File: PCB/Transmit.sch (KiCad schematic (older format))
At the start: 1 part

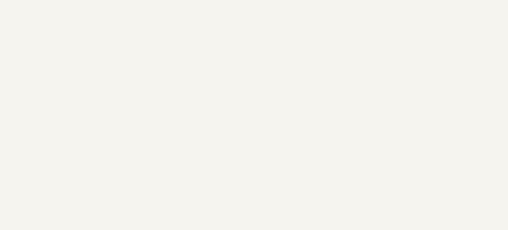
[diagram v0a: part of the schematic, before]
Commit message: Add diode pair to library
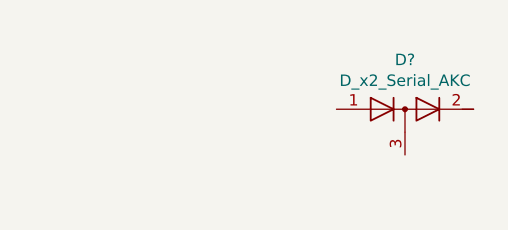
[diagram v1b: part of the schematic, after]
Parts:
- added D?: D_x2_Serial_AKC, Parts:MMBD7000L, symbol Device:D_x2_Serial_AKC
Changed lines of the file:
@@
 $Descr A4 11693 8268
 encoding utf-8
-Sheet 6 7
+Sheet 6 8
 Title ""
 Date ""
@@
 	1    0    0    -1
 $EndComp
+$Comp
+L Device:D_x2_Serial_AKC D?
+U 1 1 5DCE8F52
+P 8550 3650
+F 0 "D?" H 8550 3866 50  0000 C CNN
+F 1 "D_x2_Serial_AKC" H 8550 3775 50  0000 C CNN
+F 2 "Parts:MMBD7000L" H 8550 3650 50  0001 C CNN
+F 3 "https://www.onsemi.com/products/discretes-drivers/diodes-rectifiers/small-signal-switching-diodes/mmbd7000l" H 8550 3650 50  0001 C CNN
+	1    8550 3650
+	1    0    0    -1
+$EndComp

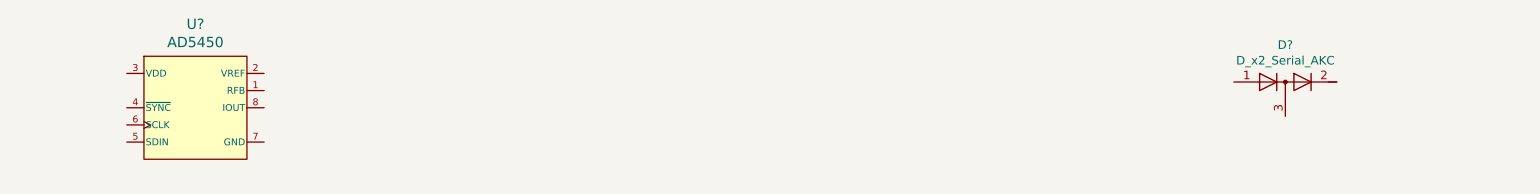
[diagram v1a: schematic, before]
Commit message: Added "near radio" warning to microcontroller pins, connected more ICs to power rails, added transducer capacitive coupling
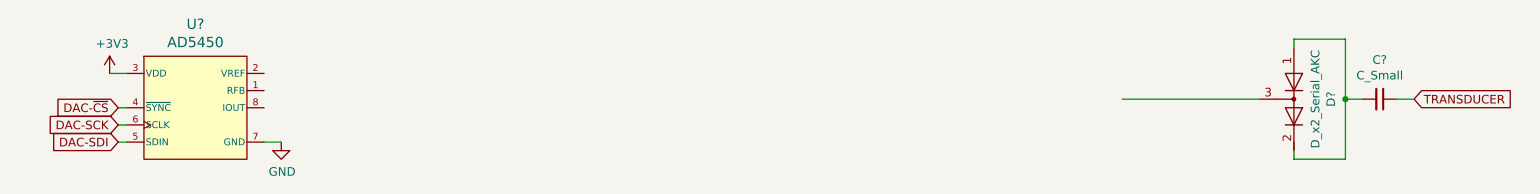
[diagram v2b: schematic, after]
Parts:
- added C?: C_Small, symbol Device:C_Small
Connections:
- net labels added: +3V3, DAC-SCK, DAC-SDI, DAC-~CS, GND, TRANSDUCER
- wire segments 0 -> 14
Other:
- moved on the sheet: D?
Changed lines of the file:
@@
 L Device:D_x2_Serial_AKC D?
 U 1 1 5DCE8F52
-P 8550 3650
-F 0 "D?" H 8550 3866 50  0000 C CNN
-F 1 "D_x2_Serial_AKC" H 8550 3775 50  0000 C CNN
-F 2 "Parts:MMBD7000L" H 8550 3650 50  0001 C CNN
-F 3 "https://www.onsemi.com/products/discretes-drivers/diodes-rectifiers/small-signal-switching-diodes/mmbd7000l" H 8550 3650 50  0001 C CNN
-	1    8550 3650
+P 8600 3750
+F 0 "D?" H 8600 3966 50  0000 C CNN
+F 1 "D_x2_Serial_AKC" H 8600 3875 50  0000 C CNN
+F 2 "Parts:MMBD7000L" H 8600 3750 50  0001 C CNN
+F 3 "https://www.onsemi.com/products/discretes-drivers/diodes-rectifiers/small-signal-switching-diodes/mmbd7000l" H 8600 3750 50  0001 C CNN
+	1    8600 3750
+	0    1    1    0
+$EndComp
+$Comp
+L power:+3V3 #PWR?
+U 1 1 5DE63453
+P 1700 3600
+F 0 "#PWR?" H 1700 3450 50  0001 C CNN
+F 1 "+3V3" H 1715 3773 50  0000 C CNN
+F 2 "" H 1700 3600 50  0001 C CNN
+F 3 "" H 1700 3600 50  0001 C CNN
+	1    1700 3600
 	1    0    0    -1
 $EndComp
+$Comp
+L power:GND #PWR?
+U 1 1 5DE63ED6
+P 2700 4000
+F 0 "#PWR?" H 2700 3750 50  0001 C CNN
+F 1 "GND" H 2705 3827 50  0000 C CNN
+F 2 "" H 2700 4000 50  0001 C CNN
+F 3 "" H 2700 4000 50  0001 C CNN
+	1    2700 4000
+	1    0    0    -1
+$EndComp
+Wire Wire Line
+	1700 3600 1800 3600
+Wire Wire Line
+	2600 4000 2700 4000
+Text GLabel 1750 3800 0    50   Input ~ 0
+DAC-~CS
+Text GLabel 1750 3900 0    50   Input ~ 0
+DAC-SCK
+Text GLabel 1750 4000 0    50   Input ~ 0
+DAC-SDI
+Wire Wire Line
+	1750 3800 1800 3800
+Wire Wire Line
+	1800 3900 1750 3900
+Wire Wire Line
+	1750 4000 1800 4000
+Wire Wire Line
+	8600 3450 8600 3400
+Wire Wire Line
+	8600 3400 8900 3400
+Wire Wire Line
+	8900 3400 8900 3750
+Wire Wire Line
+	8600 4100 8600 4050
+$Comp
+L Device:C_Small C?
+U 1 1 5DE7A1A8
+P 9100 3750
+F 0 "C?" V 8871 3750 50  0000 C CNN
+F 1 "C_Small" V 8962 3750 50  0000 C CNN
+F 2 "" H 9100 3750 50  0001 C CNN
+F 3 "~" H 9100 3750 50  0001 C CNN
+	1    9100 3750
+	0    1    1    0
+$EndComp
+Wire Wire Line
+	8900 3750 9000 3750
+Wire Wire Line
+	8600 4100 8900 4100
+Wire Wire Line
+	8900 4100 8900 3750
+Connection ~ 8900 3750
+Text GLabel 9300 3750 2    50   Input ~ 0
+TRANSDUCER
+Wire Wire Line
+	9200 3750 9300 3750
+Wire Wire Line
+	8400 3750 7600 3750
 $EndSCHEMATC

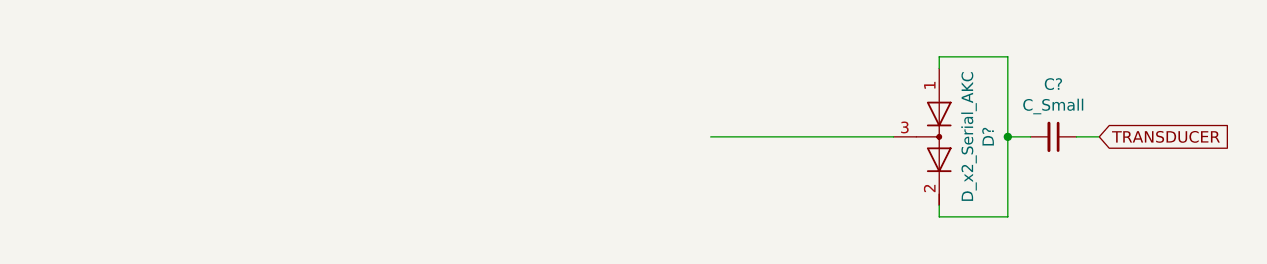
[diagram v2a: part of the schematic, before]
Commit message: Add high-voltage transmit amplifier to library
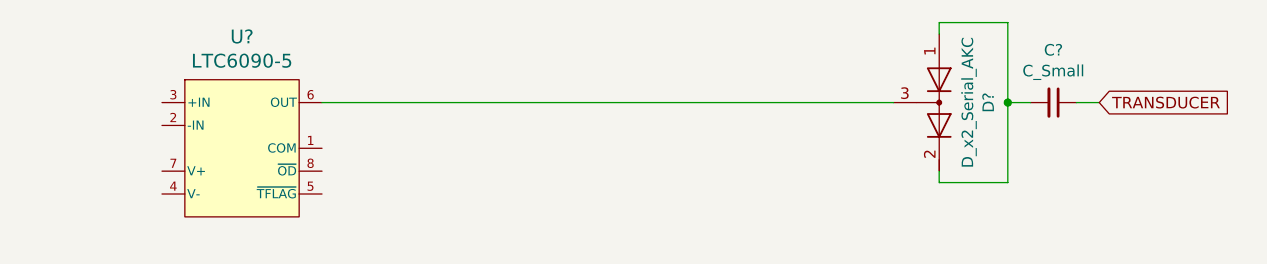
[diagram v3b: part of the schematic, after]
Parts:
- added U?: LTC6090-5, Parts:SOIC8-PAD, symbol Parts:LTC6090-5
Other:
- moved on the sheet: C?, D?
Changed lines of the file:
@@
 L Device:D_x2_Serial_AKC D?
 U 1 1 5DCE8F52
-P 8600 3750
-F 0 "D?" H 8600 3966 50  0000 C CNN
-F 1 "D_x2_Serial_AKC" H 8600 3875 50  0000 C CNN
-F 2 "Parts:MMBD7000L" H 8600 3750 50  0001 C CNN
-F 3 "https://www.onsemi.com/products/discretes-drivers/diodes-rectifiers/small-signal-switching-diodes/mmbd7000l" H 8600 3750 50  0001 C CNN
-	1    8600 3750
+P 8600 3600
+F 0 "D?" H 8600 3816 50  0000 C CNN
+F 1 "D_x2_Serial_AKC" H 8600 3725 50  0000 C CNN
+F 2 "Parts:MMBD7000L" H 8600 3600 50  0001 C CNN
+F 3 "https://www.onsemi.com/products/discretes-drivers/diodes-rectifiers/small-signal-switching-diodes/mmbd7000l" H 8600 3600 50  0001 C CNN
+	1    8600 3600
 	0    1    1    0
 $EndComp
@@
 	1750 4000 1800 4000
 Wire Wire Line
-	8600 3450 8600 3400
+	8600 3300 8600 3250
 Wire Wire Line
-	8600 3400 8900 3400
+	8600 3250 8900 3250
 Wire Wire Line
-	8900 3400 8900 3750
+	8900 3250 8900 3600
 Wire Wire Line
-	8600 4100 8600 4050
+	8600 3950 8600 3900
 $Comp
 L Device:C_Small C?
 U 1 1 5DE7A1A8
-P 9100 3750
-F 0 "C?" V 8871 3750 50  0000 C CNN
-F 1 "C_Small" V 8962 3750 50  0000 C CNN
-F 2 "" H 9100 3750 50  0001 C CNN
-F 3 "~" H 9100 3750 50  0001 C CNN
-	1    9100 3750
+P 9100 3600
+F 0 "C?" V 8871 3600 50  0000 C CNN
+F 1 "C_Small" V 8962 3600 50  0000 C CNN
+F 2 "" H 9100 3600 50  0001 C CNN
+F 3 "~" H 9100 3600 50  0001 C CNN
+	1    9100 3600
 	0    1    1    0
 $EndComp
 Wire Wire Line
-	8900 3750 9000 3750
+	8900 3600 9000 3600
 Wire Wire Line
-	8600 4100 8900 4100
+	8600 3950 8900 3950
 Wire Wire Line
-	8900 4100 8900 3750
-Connection ~ 8900 3750
-Text GLabel 9300 3750 2    50   Input ~ 0
+	8900 3950 8900 3600
+Connection ~ 8900 3600
+Text GLabel 9300 3600 2    50   Input ~ 0
 TRANSDUCER
 Wire Wire Line
-	9200 3750 9300 3750
+	9200 3600 9300 3600
 Wire Wire Line
-	8400 3750 7600 3750
+	8400 3600 5900 3600
+$Comp
+L Parts:LTC6090-5 U?
+U 1 1 5E088DE1
+P 5550 3800
+F 0 "U?" H 5550 4287 60  0000 C CNN
+F 1 "LTC6090-5" H 5550 4181 60  0000 C CNN
+F 2 "Parts:SOIC8-PAD" H 5550 3350 60  0001 C CNN
+F 3 "https://www.analog.com/en/products/ltc6090.html" H 5200 4000 60  0001 C CNN
+	1    5550 3800
+	1    0    0    -1
+$EndComp
 $EndSCHEMATC

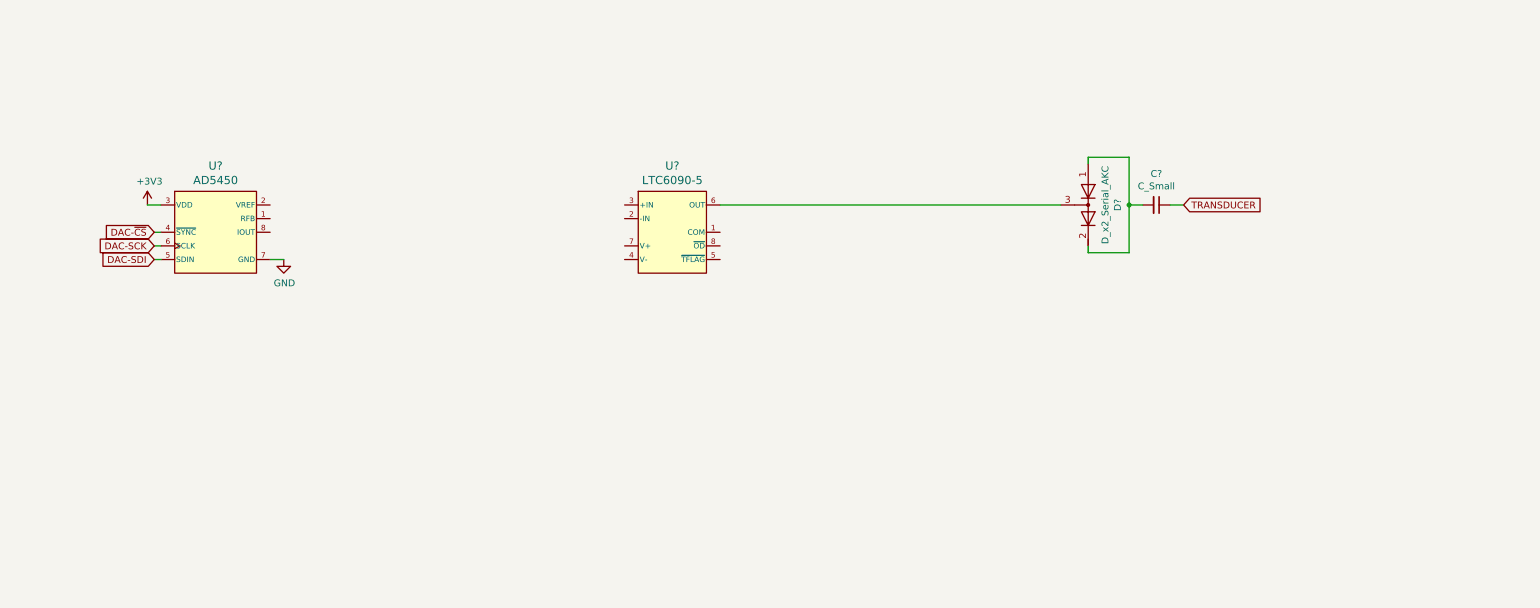
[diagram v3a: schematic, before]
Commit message: Add transmit preamplifier to library and schematic
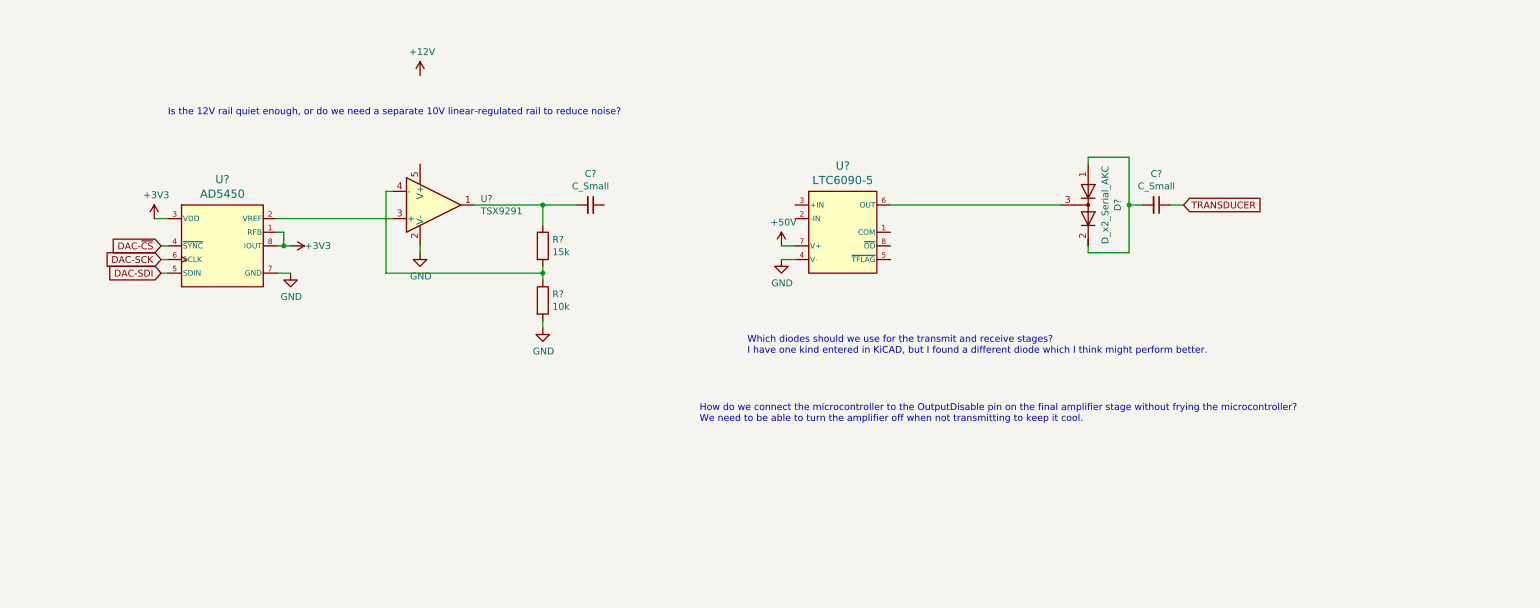
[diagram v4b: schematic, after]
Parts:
- added C?: C_Small, symbol Device:C_Small
- added R?: 10k, Resistors_SMD:R_0603_HandSoldering, symbol Device:R
- added R?: 15k, Resistors_SMD:R_0603_HandSoldering, symbol Device:R
- added U?: TSX9291, Parts:SOT23-5, symbol Parts:TSX9291
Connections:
- net +3V3: now also U?.1 (RFB), U?.8 (IOUT)
- net GND: now also U?.4 (V-), U?.9 (EPAD), R?.2, U?.2 (V-)
- net at U?.2 (VREF): now also U?.3 (+)
- net +50V: now reaches U?.7 (V+)
- new net: C?.2, R?.1, U?.1
- new net: R?.1, R?.2, U?.4 (-)
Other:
- note added: "How do we connect the microcontroller to the OutputDisable pin on the final amplifier stage without frying the microcontroller?\nWe need to be able to turn the amplifier off when not transmitting to keep it cool."
- note added: "Is the 12V rail quiet enough, or do we need a separate 10V linear-regulated rail to reduce noise?"
- note added: "Which diodes should we use for the transmit and receive stages?\nI have one kind entered in KiCAD, but I found a different diode which I think might perform better."
- moved on the sheet: U?
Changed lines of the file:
@@
 L Parts:AD5450 U?
 U 1 1 5DCE2712
-P 2200 3800
-F 0 "U?" H 2200 4287 60  0000 C CNN
-F 1 "AD5450" H 2200 4181 60  0000 C CNN
-F 2 "Parts:TSOT8" H 2200 3450 60  0001 C CNN
-F 3 "https://www.analog.com/en/products/ad5450.html" H 1800 4000 60  0001 C CNN
-	1    2200 3800
+P 2250 3900
+F 0 "U?" H 2250 4387 60  0000 C CNN
+F 1 "AD5450" H 2250 4281 60  0000 C CNN
+F 2 "Parts:TSOT8" H 2250 3550 60  0001 C CNN
+F 3 "https://www.analog.com/en/products/ad5450.html" H 1850 4100 60  0001 C CNN
+	1    2250 3900
 	1    0    0    -1
 $EndComp
@@
 L power:+3V3 #PWR?
 U 1 1 5DE63453
-P 1700 3600
-F 0 "#PWR?" H 1700 3450 50  0001 C CNN
-F 1 "+3V3" H 1715 3773 50  0000 C CNN
-F 2 "" H 1700 3600 50  0001 C CNN
-F 3 "" H 1700 3600 50  0001 C CNN
-	1    1700 3600
+P 1750 3700
+F 0 "#PWR?" H 1750 3550 50  0001 C CNN
+F 1 "+3V3" H 1765 3873 50  0000 C CNN
+F 2 "" H 1750 3700 50  0001 C CNN
+F 3 "" H 1750 3700 50  0001 C CNN
+	1    1750 3700
 	1    0    0    -1
 $EndComp
@@
 L power:GND #PWR?
 U 1 1 5DE63ED6
-P 2700 4000
-F 0 "#PWR?" H 2700 3750 50  0001 C CNN
-F 1 "GND" H 2705 3827 50  0000 C CNN
-F 2 "" H 2700 4000 50  0001 C CNN
-F 3 "" H 2700 4000 50  0001 C CNN
-	1    2700 4000
-	1    0    0    -1
-$EndComp
-Wire Wire Line
-	1700 3600 1800 3600
-Wire Wire Line
-	2600 4000 2700 4000
-Text GLabel 1750 3800 0    50   Input ~ 0
+P 2750 4100
+F 0 "#PWR?" H 2750 3850 50  0001 C CNN
+F 1 "GND" H 2755 3927 50  0000 C CNN
+F 2 "" H 2750 4100 50  0001 C CNN
+F 3 "" H 2750 4100 50  0001 C CNN
+	1    2750 4100
+	1    0    0    -1
+$EndComp
+Wire Wire Line
+	1750 3700 1850 3700
+Wire Wire Line
+	2650 4100 2750 4100
+Text GLabel 1800 3900 0    50   Input ~ 0
 DAC-~CS
-Text GLabel 1750 3900 0    50   Input ~ 0
+Text GLabel 1800 4000 0    50   Input ~ 0
 DAC-SCK
-Text GLabel 1750 4000 0    50   Input ~ 0
+Text GLabel 1800 4100 0    50   Input ~ 0
 DAC-SDI
 Wire Wire Line
-	1750 3800 1800 3800
-Wire Wire Line
-	1800 3900 1750 3900
-Wire Wire Line
-	1750 4000 1800 4000
+	1800 3900 1850 3900
+Wire Wire Line
+	1850 4000 1800 4000
+Wire Wire Line
+	1800 4100 1850 4100
 Wire Wire Line
 	8600 3300 8600 3250
@@
 	9200 3600 9300 3600
 Wire Wire Line
-	8400 3600 5900 3600
+	8400 3600 7150 3600
 $Comp
 L Parts:LTC6090-5 U?
 U 1 1 5E088DE1
-P 5550 3800
-F 0 "U?" H 5550 4287 60  0000 C CNN
-F 1 "LTC6090-5" H 5550 4181 60  0000 C CNN
-F 2 "Parts:SOIC8-PAD" H 5550 3350 60  0001 C CNN
-F 3 "https://www.analog.com/en/products/ltc6090.html" H 5200 4000 60  0001 C CNN
-	1    5550 3800
-	1    0    0    -1
+P 6800 3800
+F 0 "U?" H 6800 4287 60  0000 C CNN
+F 1 "LTC6090-5" H 6800 4181 60  0000 C CNN
+F 2 "Parts:SOIC8-PAD" H 6800 3350 60  0001 C CNN
+F 3 "https://www.analog.com/en/products/ltc6090.html" H 6450 4000 60  0001 C CNN
+	1    6800 3800
+	1    0    0    -1
+$EndComp
+$Comp
+L Parts:+50V #PWR?
+U 1 1 5DEC98C8
+P 6350 3900
+F 0 "#PWR?" H 6350 3750 50  0001 C CNN
+F 1 "+50V" H 6365 4073 50  0000 C CNN
+F 2 "" H 6350 3900 50  0001 C CNN
+F 3 "" H 6350 3900 50  0001 C CNN
+	1    6350 3900
+	1    0    0    -1
+$EndComp
+Wire Wire Line
+	6350 3900 6450 3900
+$Comp
+L power:GND #PWR?
+U 1 1 5DECB29F
+P 6350 4000
+F 0 "#PWR?" H 6350 3750 50  0001 C CNN
+F 1 "GND" H 6355 3827 50  0000 C CNN
+F 2 "" H 6350 4000 50  0001 C CNN
+F 3 "" H 6350 4000 50  0001 C CNN
+	1    6350 4000
+	1    0    0    -1
+$EndComp
+Wire Wire Line
+	6350 4000 6450 4000
+$Comp
+L Parts:TSX9291 U?
+U 1 1 5DED28E6
+P 3800 3600
+F 0 "U?" H 4144 3646 50  0000 L CNN
+F 1 "TSX9291" H 4144 3555 50  0000 L CNN
+F 2 "Parts:SOT23-5" H 3700 3400 50  0001 L CNN
+F 3 "https://www.st.com/content/st_com/en/products/amplifiers-and-comparators/operational-amplifiers-op-amps/precision-op-amps-lt50-mhz/rail-to-rail-op-amps/tsx9291.html" H 3950 3750 50  0001 C CNN
+	1    3800 3600
+	1    0    0    -1
+$EndComp
+$Comp
+L power:GND #PWR?
+U 1 1 5DED523B
+P 3700 3950
+F 0 "#PWR?" H 3700 3700 50  0001 C CNN
+F 1 "GND" H 3705 3777 50  0000 C CNN
+F 2 "" H 3700 3950 50  0001 C CNN
+F 3 "" H 3700 3950 50  0001 C CNN
+	1    3700 3950
+	1    0    0    -1
+$EndComp
+$Comp
+L power:+12V #PWR?
+U 1 1 5DED5B08
+P 3700 2650
+F 0 "#PWR?" H 3700 2500 50  0001 C CNN
+F 1 "+12V" H 3715 2823 50  0000 C CNN
+F 2 "" H 3700 2650 50  0001 C CNN
+F 3 "" H 3700 2650 50  0001 C CNN
+	1    3700 2650
+	1    0    0    -1
+$EndComp
+Text Notes 1850 2950 0    50   ~ 0
+Is the 12V rail quiet enough, or do we need a separate 10V linear-regulated rail to reduce noise?
+$Comp
+L Device:R R?
+U 1 1 5DEDD2CE
+P 4600 4300
+F 0 "R?" H 4670 4346 50  0000 L CNN
+F 1 "10k" H 4670 4255 50  0000 L CNN
+F 2 "Resistors_SMD:R_0603_HandSoldering" V 4530 4300 50  0001 C CNN
+F 3 "https://www.digikey.ca/product-detail/en/stackpole-electronics-inc/RMCF0603FT10K0/RMCF0603FT10K0CT-ND/1943057" H 4600 4300 50  0001 C CNN
+	1    4600 4300
+	1    0    0    -1
+$EndComp
+$Comp
+L power:GND #PWR?
+U 1 1 5DEDEBA9
+P 4600 4500
+F 0 "#PWR?" H 4600 4250 50  0001 C CNN
+F 1 "GND" H 4605 4327 50  0000 C CNN
+F 2 "" H 4600 4500 50  0001 C CNN
+F 3 "" H 4600 4500 50  0001 C CNN
+	1    4600 4500
+	1    0    0    -1
+$EndComp
+$Comp
+L Device:R R?
+U 1 1 5DEDF69F
+P 4600 3900
+F 0 "R?" H 4670 3946 50  0000 L CNN
+F 1 "15k" H 4670 3855 50  0000 L CNN
+F 2 "Resistors_SMD:R_0603_HandSoldering" V 4530 3900 50  0001 C CNN
+F 3 "https://www.digikey.ca/product-detail/en/stackpole-electronics-inc/RMCF0603FT15K0/RMCF0603FT15K0CT-ND/1943069" H 4600 3900 50  0001 C CNN
+	1    4600 3900
+	1    0    0    -1
+$EndComp
+Wire Wire Line
+	4600 4450 4600 4500
+Wire Wire Line
+	4600 4150 4600 4100
+Wire Wire Line
+	3500 3500 3450 3500
+Wire Wire Line
+	3450 3500 3450 4100
+Wire Wire Line
+	3450 4100 4600 4100
+Wire Wire Line
+	4600 4100 4600 4050
+Wire Wire Line
+	3700 3900 3700 3950
+Connection ~ 4600 4100
+Wire Wire Line
+	4100 3600 4600 3600
+Wire Wire Line
+	4600 3600 4600 3750
+Connection ~ 4600 3600
+Wire Wire Line
+	4600 3600 4850 3600
+Wire Wire Line
+	2650 3800 2700 3800
+Wire Wire Line
+	2700 3800 2700 3900
+Wire Wire Line
+	2700 3900 2650 3900
+$Comp
+L power:+3V3 #PWR?
+U 1 1 5DEEBC70
+P 2750 3900
+F 0 "#PWR?" H 2750 3750 50  0001 C CNN
+F 1 "+3V3" V 2750 4100 50  0000 C CNN
+F 2 "" H 2750 3900 50  0001 C CNN
+F 3 "" H 2750 3900 50  0001 C CNN
+	1    2750 3900
+	0    1    1    0
+$EndComp
+Wire Wire Line
+	2700 3900 2750 3900
+Connection ~ 2700 3900
+Wire Wire Line
+	2650 3700 3500 3700
+Text Notes 6100 4700 0    50   ~ 0
+Which diodes should we use for the transmit and receive stages?\nI have one kind entered in KiCAD, but I found a different diode which I think might perform better.
+Text Notes 5750 5200 0    50   ~ 0
+How do we connect the microcontroller to the OutputDisable pin on the final amplifier stage without frying the microcontroller?\nWe need to be able to turn the amplifier off when not transmitting to keep it cool.
+$Comp
+L Device:C_Small C?
+U 1 1 5DF03C94
+P 4950 3600
+F 0 "C?" V 4721 3600 50  0000 C CNN
+F 1 "C_Small" V 4812 3600 50  0000 C CNN
+F 2 "" H 4950 3600 50  0001 C CNN
+F 3 "~" H 4950 3600 50  0001 C CNN
+	1    4950 3600
+	0    1    1    0
 $EndComp
 $EndSCHEMATC

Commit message: Additional note
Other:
- note added: "Also need to generate mid-rail for 50V amplifier"
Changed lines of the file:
@@
 	0    1    1    0
 $EndComp
+Text Notes 4900 5850 0    50   ~ 0
+Also need to generate mid-rail for 50V amplifier
 $EndSCHEMATC
